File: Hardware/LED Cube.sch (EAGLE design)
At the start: 140 parts, among them IC1 MEGA32-P, IC10 FT232RL, IC11 FM24V10, IC12 MSGEQ7, IC13 MEGA8-P, IC2 74HC573N, IC3 74HC573N, IC4 74HC573N, IC5 74HC573N, IC6 74HC573N, IC7 74HC573N, IC8 74HC573N, IC9 74HC573N, Q2 BUZ382, Q3 BUZ382, Q4 BUZ382, Q5 BUZ382, Q6 BUZ382, Q7 BUZ382, Q8 BUZ382, Q9 BUZ382

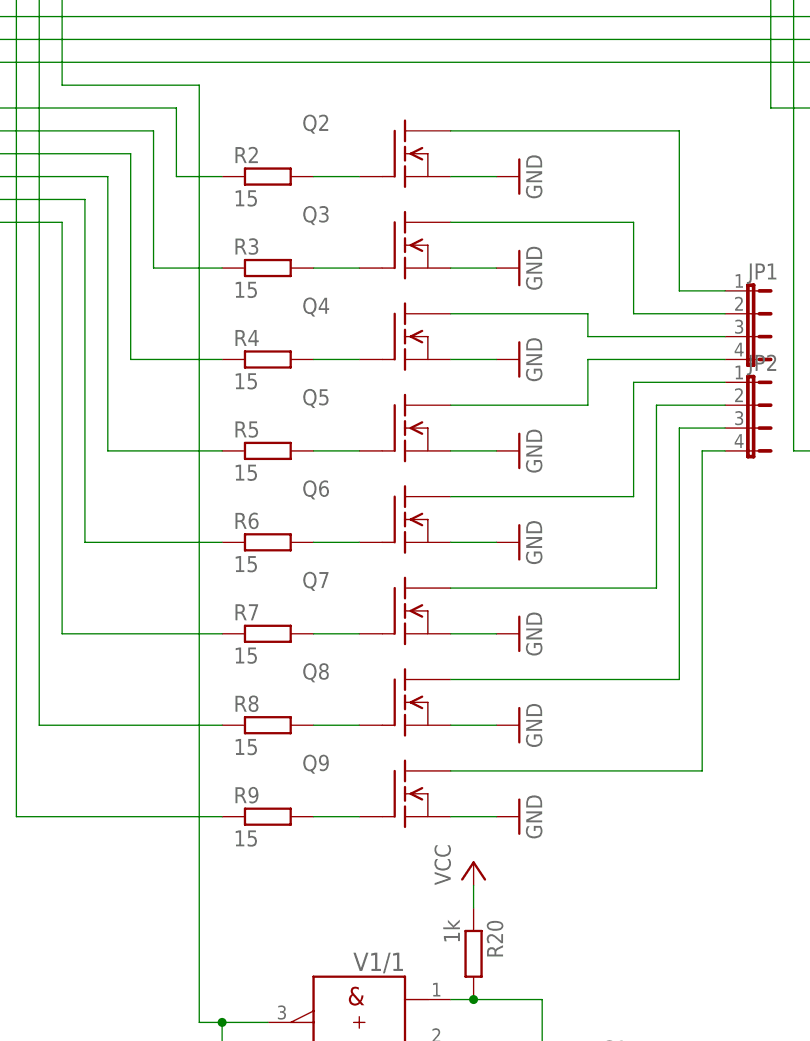
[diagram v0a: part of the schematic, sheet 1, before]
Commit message: Fixed MOSFET Problems
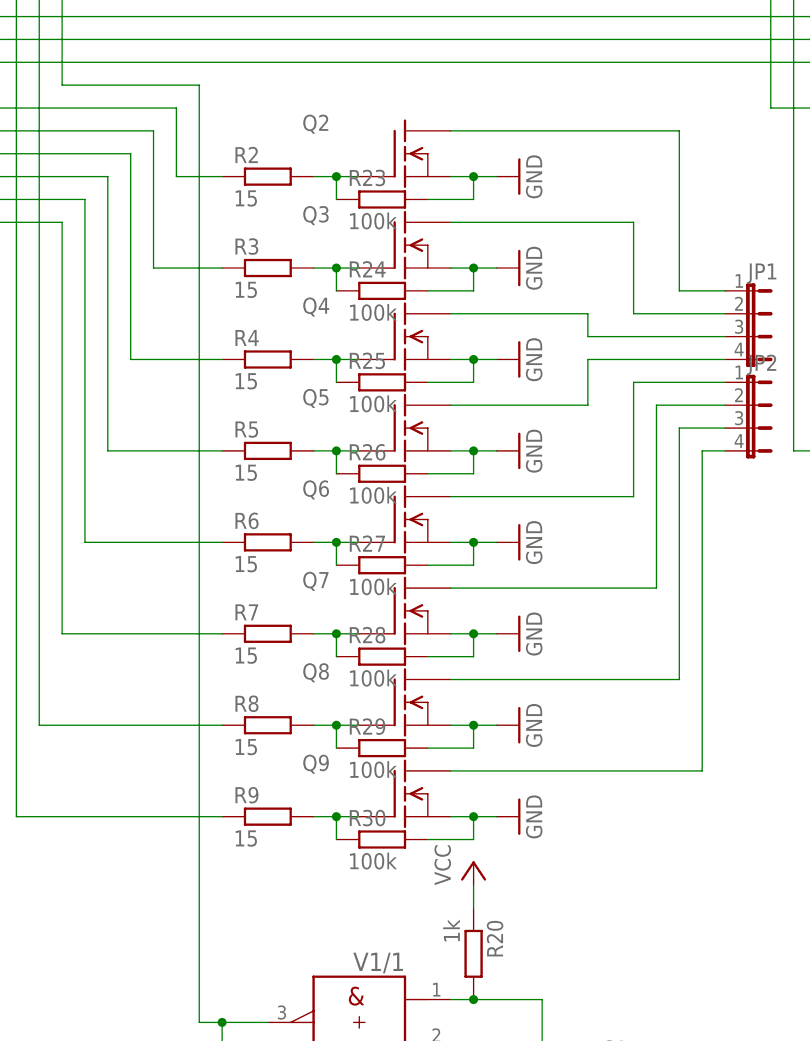
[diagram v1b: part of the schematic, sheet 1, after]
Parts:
- added R23, R24, R25, R26, R27, R28, R29, R30: 100k, resistor:R-EU_0204/7
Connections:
- net GND: now also R23.2, R24.2, R25.2, R26.2, R27.2, R28.2, R29.2, R30.2
- net N$22: now also R23.1
- net N$31: now also R24.1
- net N$32: now also R25.1
- net N$33: now also R26.1
- net N$34: now also R27.1
- net N$35: now also R28.1
- net N$36: now also R29.1
- net N$37: now also R30.1

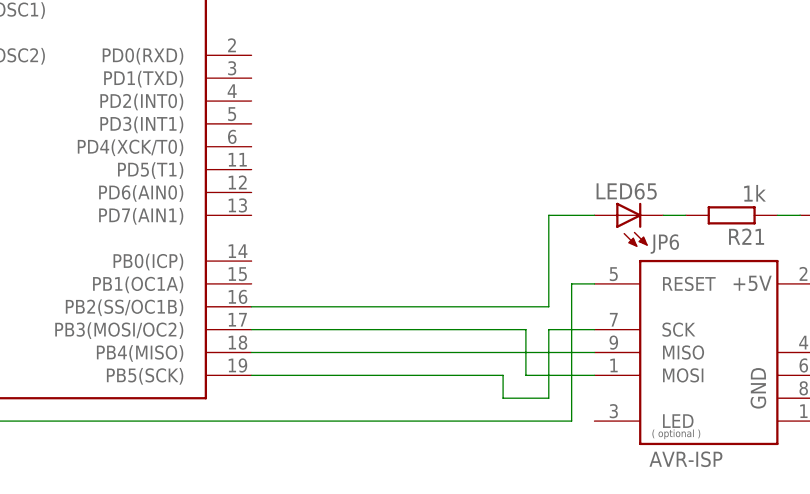
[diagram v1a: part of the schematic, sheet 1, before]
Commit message: Audio detection working
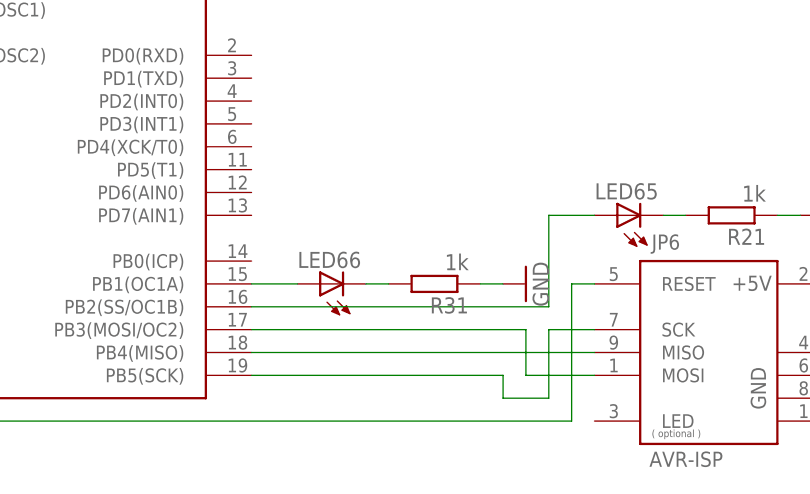
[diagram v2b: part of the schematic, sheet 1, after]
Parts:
- added LED66: (no value), led:LED5MM
- added R31: 1k, resistor:R-EU_0204/7
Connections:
- new net N$82: IC13.PB1(OC1A), LED66.A
- new net N$83: LED66.C, R31.2
- net GND: now also R31.1
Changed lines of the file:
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@@
 <setting verticaltext="up"/>
 </settings>
-<grid distance="0.1" unitdist="inch" unit="inch" style="lines" multiple="1" display="no" altdistance="0.05" altunitdist="inch" altunit="inch"/>
+<grid distance="0.1" unitdist="inch" unit="inch" style="lines" multiple="1" display="no" altdistance="0.01" altunitdist="inch" altunit="inch"/>
 <layers>
 <layer number="1" name="Top" color="4" fill="1" visible="no" active="no"/>
@@
 <part name="R29" library="resistor" deviceset="R-EU_" device="0204/7" value="100k"/>
 <part name="R30" library="resistor" deviceset="R-EU_" device="0204/7" value="100k"/>
+<part name="LED66" library="led" deviceset="LED" device="5MM"/>
+<part name="R31" library="resistor" deviceset="R-EU_" device="0204/7" value="1k"/>
+<part name="GND38" library="supply1" deviceset="GND" device=""/>
 </parts>
 <sheets>
@@
 <instance part="R29" gate="G$1" x="88.9" y="-43.18"/>
 <instance part="R30" gate="G$1" x="88.9" y="-53.34"/>
+<instance part="LED66" gate="G$1" x="-17.78" y="-124.46" rot="R90"/>
+<instance part="R31" gate="G$1" x="-5.08" y="-124.46" rot="R180"/>
+<instance part="GND38" gate="1" x="5.08" y="-124.46" rot="R90"/>
 </instances>
 <busses>
@@
 <pinref part="GND37" gate="1" pin="GND"/>
 <pinref part="R22" gate="G$1" pin="A"/>
+</segment>
+<segment>
+<pinref part="R31" gate="G$1" pin="1"/>
+<pinref part="GND38" gate="1" pin="GND"/>
+<wire x1="0" y1="-124.46" x2="2.54" y2="-124.46" width="0.1524" layer="91"/>
 </segment>
 </net>
@@
 </segment>
 </net>
+<net name="N$82" class="0">
+<segment>
+<pinref part="IC13" gate="G$1" pin="PB1(OC1A)"/>
+<pinref part="LED66" gate="G$1" pin="A"/>
+<wire x1="-25.4" y1="-124.46" x2="-20.32" y2="-124.46" width="0.1524" layer="91"/>
+</segment>
+</net>
+<net name="N$83" class="0">
+<segment>
+<pinref part="LED66" gate="G$1" pin="C"/>
+<pinref part="R31" gate="G$1" pin="2"/>
+<wire x1="-12.7" y1="-124.46" x2="-10.16" y2="-124.46" width="0.1524" layer="91"/>
+</segment>
+</net>

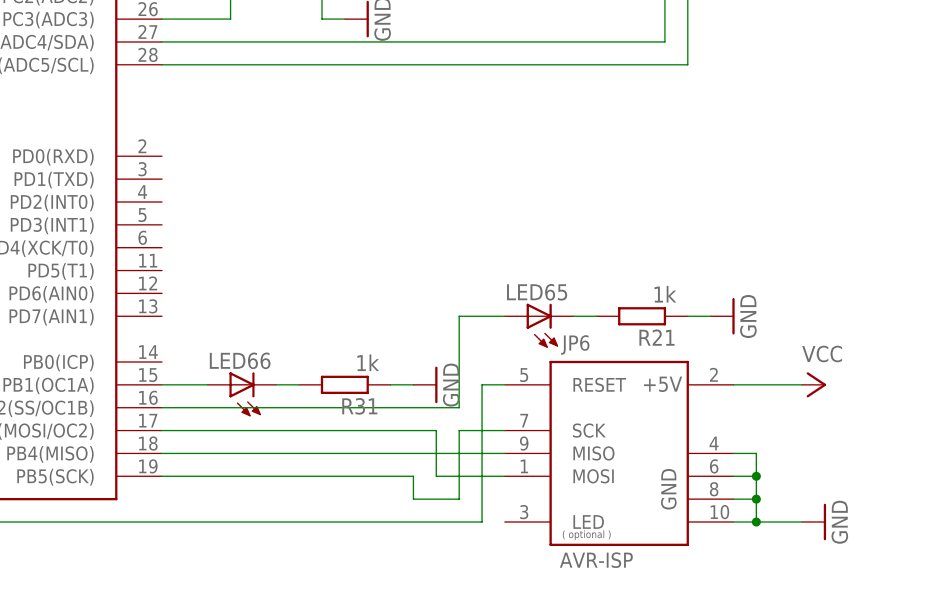
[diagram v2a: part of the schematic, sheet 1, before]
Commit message: Added LEDs to Audio Device
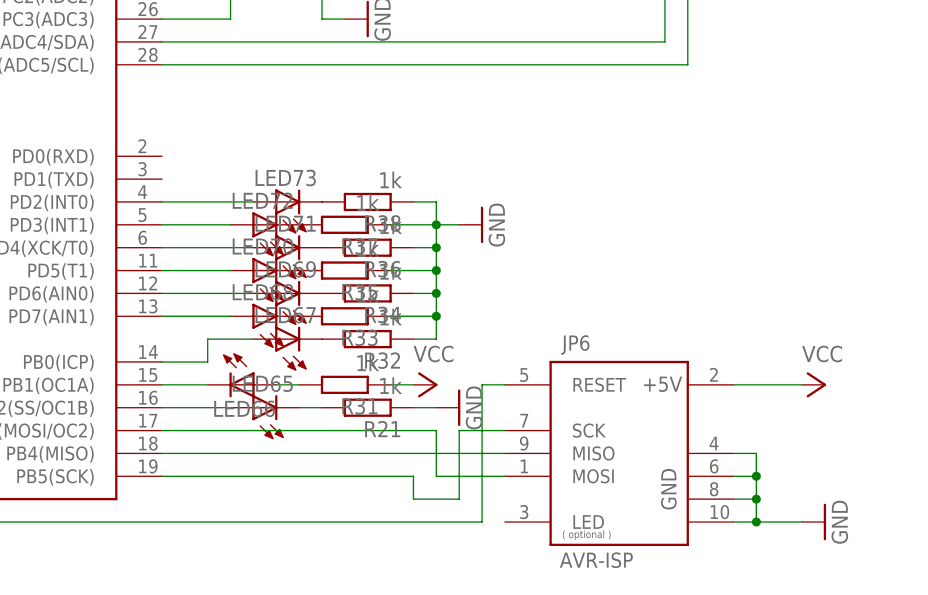
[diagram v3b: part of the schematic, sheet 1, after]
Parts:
- added LED67, LED68, LED69, LED70, LED71, LED72, LED73: (no value), led:LED5MM
- added R32, R33, R34, R35, R36, R37, R38: 1k, resistor:R-EU_0204/7
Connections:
- new net N$84: LED67.C, R32.2
- new net N$85: LED68.C, R33.2
- new net N$86: LED69.C, R34.2
- new net N$87: LED70.C, R35.2
- new net N$88: LED71.C, R36.2
- new net N$89: LED72.C, R37.2
- new net N$90: LED73.C, R38.2
- new net N$91: IC13.PB0(ICP), LED67.A
- new net N$92: IC13.PD7(AIN1), LED68.A
- new net N$93: IC13.PD6(AIN0), LED69.A
- new net N$94: IC13.PD5(T1), LED70.A
- new net N$95: IC13.PD4(XCK/T0), LED71.A
- new net N$96: IC13.PD3(INT1), LED72.A
- new net N$97: IC13.PD2(INT0), LED73.A
- net GND: now also R32.1, R33.1, R34.1, R35.1, R36.1, R37.1, R38.1; no longer R31.1
- net N$82: now also R31.2; no longer IC13.PB1(OC1A)
- net N$83: now also IC13.PB1(OC1A); no longer R31.2
- net VCC: now also R31.1
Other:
- moved on the sheet: LED65, LED66, R21

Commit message: Schematic ready for layout creation
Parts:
- removed CON1: (no value), con-harting:CON64
- removed IC13: MEGA8-P, 0-avr-6:MEGA8-P
- removed JP4, JP5: (no value), jumper:JP4E
- removed LED10, LED11, LED12, LED13, LED14, LED15, LED16, LED17, LED18, LED19, LED2, LED20, LED21, LED22, LED23, LED24, LED25, LED26, LED27, LED28, LED29, LED3, LED30, LED31, LED32, LED33, LED34, LED35, LED36, LED37, LED38, LED39, LED4, LED40, LED41, LED42, LED43, LED44, LED45, LED46, LED47, LED48, LED49, LED5, LED50, LED51, LED52, LED53, LED54, LED55, LED56, LED57, LED58, LED59, LED6, LED60, LED61, LED62, LED63, LED64, LED7, LED8, LED9: (no value), led:LED3MM
- removed LED66: (no value), led:LED5MM
- removed X1: (no value), con-berg:PN61729
- added IC14: MEGA32-A, atmel:MEGA32-A
- added R100, R101, R102, R39, R40, R41, R42, R43, R44, R45, R46, R47, R48, R49, R50, R51, R52, R53, R54, R55, R56, R57, R58, R59, R60, R61, R62, R63, R64, R65, R66, R67, R68, R69, R70, R71, R72, R73, R74, R75, R76, R77, R78, R79, R80, R81, R82, R83, R84, R85, R86, R87, R88, R89, R90, R91, R92, R93, R94, R95, R96, R97, R98, R99: 1k, resistor:R-EU_R0603
- added SV1: (no value), con-ml:ML64
- added U$10, U$11, U$12, U$13, U$14, U$15, U$16, U$17, U$18, U$19, U$20, U$21, U$22, U$23, U$24, U$25, U$26, U$27, U$28, U$29, U$3, U$30, U$31, U$32, U$33, U$34, U$35, U$36, U$37, U$38, U$39, U$4, U$40, U$41, U$42, U$43, U$44, U$45, U$46, U$47, U$48, U$49, U$5, U$50, U$51, U$52, U$53, U$54, U$55, U$56, U$57, U$58, U$59, U$6, U$60, U$61, U$62, U$63, U$64, U$65, U$7, U$8, U$9: PNP, 0-xythobuz:PNP
- added X2: USB-B-MINI-SMD, 1_USER:USB-B-MINI-SMD
- C1, C2, C3, C4, C5: device resistor:C-EU050-030X075 -> resistor:C-EUC0603
- C10, C11, C12, C13, C14, C15, C16, C17, C18, C6, C7, C8, C9: device resistor:C-EU050-025X075 -> resistor:C-EUC0603
- IC1: value MEGA32-P -> MEGA8-AI; device 0-avr-6:MEGA32-P -> atmel:MEGA8-AI
- IC2, IC3, IC4, IC5, IC6, IC7, IC8, IC9: value 74HC573N -> 74HC573D; device 74xx-eu:74HC573N -> 74xx-eu:74HC573D
- LED1: device led:LED3MM -> led:LEDCHIPLED_0603
- LED65, LED67, LED68, LED69, LED70, LED71, LED72, LED73: device led:LED5MM -> led:LEDCHIPLED_0603
- R1, R10, R11, R12, R13, R14, R15, R16, R17, R18, R19, R2, R20, R23, R24, R25, R26, R27, R28, R29, R3, R30, R4, R5, R6, R7, R8, R9: device resistor:R-EU_0204/7 -> resistor:R-EU_R0603
- U$2: value KLINKENBUCHSE -> PNP; device 0-xythobuz:KLINKENBUCHSE -> 0-xythobuz:PNP
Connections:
- removed net LEDA1: CON1.1, LED15.A
- removed net LEDA2: CON1.2, LED14.A
- removed net LEDA3: CON1.3, LED13.A
- removed net LEDA4: CON1.4, LED12.A
- removed net LEDA5: CON1.5, LED11.A
- removed net LEDA6: CON1.6, LED10.A
- removed net LEDA7: CON1.7, LED9.A
- removed net LEDA8: CON1.8, LED8.A
- new net N$100: SV1.5, U$4.C
- new net N$101: R44.2, U$7.B
- new net N$102: SV1.6, U$7.C
- new net N$103: R42.2, U$5.B
- new net N$104: SV1.8, U$9.C
- new net N$105: SV1.16, U$17.C
- new net N$106: R63.2, U$26.B
- new net N$107: R64.2, U$27.B
- new net N$108: R65.2, U$28.B
- new net N$109: SV1.12, U$11.C
- new net N$110: SV1.10, U$13.C
- new net N$111: SV1.9, U$10.C
- new net N$112: R54.2, U$17.B
- new net N$113: R63.1
- new net N$114: R64.1
- new net N$115: R66.2, U$29.B
- new net N$116: R66.1
- new net N$117: R67.2, U$30.B
- new net N$118: R67.1
- new net N$119: R65.1
- new net N$120: R68.2, U$31.B
- new net N$121: R71.2, U$34.B
- new net N$122: R72.2, U$35.B
- new net N$123: R73.2, U$36.B
- new net N$124: R71.1
- new net N$125: R72.1
- new net N$126: R74.2, U$37.B
- new net N$127: R74.1
- new net N$128: R75.2, U$38.B
- new net N$130: SV1.63, U$64.C
- new net N$131: SV1.61, U$60.C
- new net N$134: SV1.62, U$63.C
- new net N$136: SV1.58, U$61.C
- new net N$137: R95.2, U$58.B
- new net N$138: SV1.55, U$56.C
- new net N$139: R96.2, U$59.B
- new net N$140: R97.2, U$60.B
- new net N$141: R95.1
- new net N$142: SV1.54, U$55.C
- new net N$143: R96.1
- new net N$144: SV1.50, U$53.C
- new net N$145: R87.2, U$50.B
- new net N$146: R88.2, U$51.B
- new net N$147: R89.2, U$52.B
- new net N$148: R87.1
- new net N$149: R88.1
- new net N$150: R90.2, U$53.B
- new net N$151: R90.1
- new net N$152: R91.2, U$54.B
- new net N$153: R79.2, U$42.B
- new net N$154: R80.2, U$43.B
- new net N$155: R81.2, U$44.B
- new net N$156: R79.1
- new net N$157: R80.1
- new net N$158: R82.2, U$45.B
- new net N$159: R82.1
- new net N$160: R83.2, U$46.B
- new net N$161: R40.2, U$3.B
- new net N$162: R39.2, U$2.B
- new net N$163: IC7A.5Q, R41.1
- new net N$164: SV1.1, U$2.C
- new net N$165: R41.2, U$4.B
- new net N$166: SV1.7, U$8.C
- new net N$167: IC7A.1Q, R39.1
- new net N$168: IC7A.4Q, R40.1
- new net N$169: R47.2, U$10.B
- new net N$170: IC7A.6Q, R44.1
- new net N$171: R45.2, U$8.B
- new net N$172: IC7A.2Q, R42.1
- new net N$173: R43.2, U$6.B
- new net N$174: R48.2, U$11.B
- new net N$175: IC7A.3Q, R43.1
- new net N$176: IC7A.7Q, R45.1
- new net N$177: R46.2, U$9.B
- new net N$178: R49.2, U$12.B
- new net N$179: IC7A.8Q, R46.1
- new net N$180: R47.1
- new net N$181: R48.1
- new net N$182: R68.1
- new net N$183: SV1.13, U$12.C
- new net N$184: R50.2, U$13.B
- new net N$185: R50.1
- new net N$186: R51.2, U$14.B
- new net N$187: R51.1
- new net N$188: SV1.11, U$14.C
- new net N$189: R49.1
- new net N$190: R69.2, U$32.B
- new net N$191: R69.1
- new net N$192: R52.2, U$15.B
- new net N$193: R52.1
- new net N$194: SV1.14, U$15.C
- new net N$195: R53.2, U$16.B
- new net N$196: R53.1
- new net N$197: SV1.15, U$16.C
- new net N$198: R70.1
- new net N$199: SV1.32, U$33.C
- new net N$200: R54.1
- new net N$201: R55.2, U$18.B
- new net N$202: R56.2, U$19.B
- new net N$203: R57.2, U$20.B
- new net N$204: R55.1
- new net N$205: R56.1
- new net N$206: R58.2, U$21.B
- new net N$207: R58.1
- new net N$208: R59.2, U$22.B
- new net N$209: R59.1
- new net N$210: R57.1
- new net N$211: R60.2, U$23.B
- new net N$212: R60.1
- new net N$213: R61.2, U$24.B
- new net N$214: R61.1
- new net N$215: R62.1
- new net N$216: SV1.24, U$25.C
- new net N$217: SV1.23, U$24.C
- new net N$218: SV1.22, U$23.C
- new net N$219: SV1.21, U$20.C
- new net N$220: SV1.20, U$19.C
- new net N$221: SV1.18, U$21.C
- new net N$222: SV1.17, U$18.C
- new net N$223: R62.2, U$25.B
- new net N$224: SV1.19, U$22.C
- new net N$225: SV1.31, U$32.C
- new net N$226: SV1.30, U$31.C
- new net N$227: SV1.29, U$28.C
- new net N$228: SV1.28, U$27.C
- new net N$229: SV1.26, U$29.C
- new net N$230: SV1.25, U$26.C
- new net N$231: R70.2, U$33.B
- new net N$232: SV1.27, U$30.C
- new net N$233: R75.1
- new net N$234: R73.1
- new net N$235: R76.2, U$39.B
- new net N$236: R76.1
- new net N$237: R77.2, U$40.B
- new net N$238: R77.1
- new net N$239: R78.1
- new net N$240: SV1.40, U$41.C
- new net N$241: SV1.39, U$40.C
- new net N$242: SV1.38, U$39.C
- new net N$243: SV1.37, U$36.C
- new net N$244: SV1.36, U$35.C
- new net N$245: SV1.34, U$37.C
- new net N$246: SV1.33, U$34.C
- new net N$247: R78.2, U$41.B
- new net N$248: SV1.35, U$38.C
- new net N$249: R83.1
- new net N$250: R81.1
- new net N$251: R84.2, U$47.B
- new net N$252: R84.1
- new net N$253: R85.2, U$48.B
- new net N$254: R85.1
- new net N$255: R86.1
- new net N$256: SV1.48, U$49.C
- new net N$257: SV1.47, U$48.C
- new net N$258: SV1.46, U$47.C
- new net N$259: SV1.45, U$44.C
- new net N$260: SV1.44, U$43.C
- new net N$261: SV1.42, U$45.C
- new net N$262: SV1.41, U$42.C
- new net N$263: R86.2, U$49.B
- new net N$264: SV1.43, U$46.C
- new net N$265: R91.1
- new net N$266: R89.1
- new net N$267: R92.2, U$55.B
- new net N$268: R92.1
- new net N$269: R93.2, U$56.B
- new net N$270: R93.1
- new net N$271: R94.1
- new net N$272: SV1.56, U$57.C
- new net N$273: R98.2, U$61.B
- new net N$274: R98.1
- new net N$275: SV1.53, U$52.C
- new net N$276: SV1.52, U$51.C
- new net N$277: R99.2, U$62.B
- new net N$278: SV1.49, U$50.C
- new net N$279: R94.2, U$57.B
- new net N$280: SV1.51, U$54.C
- new net N$281: R99.1
- new net N$282: R97.1
- new net N$283: R100.2, U$63.B
- new net N$284: R100.1
- new net N$285: R101.2, U$64.B
- new net N$286: R101.1
- new net N$287: R102.1
- new net N$288: SV1.64, U$65.C
- new net N$292: SV1.60, U$59.C
- new net N$294: SV1.57, U$58.C
- new net N$295: R102.2, U$65.B
- new net N$296: SV1.59, U$62.C
- new net N$98: SV1.2, U$5.C
- new net N$99: SV1.3, U$6.C
- net GND: now also IC1.GND@1, IC1.GND@2, IC14.GND, IC14.GND1, IC14.GND2, IC14.GND@1, R31.1, X2-CON.5; no longer IC1.AGND, IC13.AGND, IC13.GND@1, U$2.GND, X1.4
- net N$1: now also SV1.4, U$3.C; no longer JP4.4, LED1.C, LED10.C, LED11.C, LED12.C, LED13.C, LED14.C, LED15.C, LED16.C, LED17.C, LED18.C, LED19.C, LED2.C, LED20.C, LED21.C, LED22.C, LED23.C, LED24.C, LED25.C, LED26.C, LED27.C, LED28.C, LED29.C, LED3.C, LED30.C, LED31.C, LED32.C, LED33.C, LED34.C, LED35.C, LED36.C, LED37.C, LED38.C, LED39.C, LED4.C, LED40.C, LED41.C, LED42.C, LED43.C, LED44.C, LED45.C, LED46.C, LED47.C, LED48.C, LED49.C, LED5.C, LED50.C, LED51.C, LED52.C, LED53.C, LED54.C, LED55.C, LED56.C, LED57.C, LED58.C, LED59.C, LED6.C, LED60.C, LED61.C, LED62.C, LED63.C, LED64.C, LED7.C, LED8.C, LED9.C
- net N$10: now also IC14.(ADC4)PA4; no longer IC1.(ADC4)PA4
- net N$11: now also IC14.(ADC5)PA5; no longer IC1.(ADC5)PA5
- net N$12: now also IC14.(ADC6)PA6; no longer IC1.(ADC6)PA6
- net N$13: now also IC14.(ADC7)PA7; no longer IC1.(ADC7)PA7
- net N$14: now also IC14.(T1)PB1; no longer IC1.(T1)PB1
- net N$15: now also IC14.(AIN0/INT2)PB2; no longer IC1.(AIN0/INT2)PB2
- net N$16: now also IC14.(TCK)PC2; no longer IC1.(TCK)PC2
- net N$17: now also IC14.(TMS)PC3; no longer IC1.(TMS)PC3
- net N$18: now also IC14.(TDO)PC4; no longer IC1.(TDO)PC4
- net N$19: now also IC14.(TDI)PC5; no longer IC1.(TDI)PC5
- net N$2: now also IC14.RESET; no longer IC1.RESET
- net N$20: now also IC14.(TOSC1)PC6; no longer IC1.(TOSC1)PC6
- net N$21: now also IC14.(TOSC2)PC7; no longer IC1.(TOSC2)PC7
- net N$23: now also IC14.(OC2)PD7; no longer IC1.(OC2)PD7
- net N$24: now also IC14.(ICP)PD6; no longer IC1.(ICP)PD6
- net N$25: now also IC14.(OC1A)PD5; no longer IC1.(OC1A)PD5
- net N$26: now also IC14.(OC1B)PD4; no longer IC1.(OC1B)PD4
- net N$27: now also IC14.(INT1)PD3; no longer IC1.(INT1)PD3
- net N$28: now also IC14.(INT0)PD2; no longer IC1.(INT0)PD2
- net N$29: now also IC14.(SS)PB4; no longer IC1.(SS)PB4
- net N$3: now also IC14.AREF; no longer IC1.AREF
- net N$30: now also IC14.(AIN1/OC0)PB3; no longer IC1.(AIN1/OC0)PB3
- net N$4: now also IC14.(ADC0)PA0; no longer IC1.(ADC0)PA0
- net N$46: now also X2-CON.1; no longer X1.1
- net N$47: now also IC14.(SCK)PB7; no longer IC1.(SCK)PB7
- net N$48: now also IC14.(MISO)PB6; no longer IC1.(MISO)PB6
- net N$49: now also IC14.(MOSI)PB5; no longer IC1.(MOSI)PB5
- net N$5: now also IC14.(ADC1)PA1; no longer IC1.(ADC1)PA1
- net N$50: now also IC14.(TXD)PD1; no longer IC1.(TXD)PD1
- net N$51: now also IC14.(RXD)PD0; no longer IC1.(RXD)PD0
- net N$53: now also IC1.PC4(ADC4/SDA), IC14.PC1(SDA); no longer IC1.(SDA)PC1, IC13.PC4(ADC4/SDA)
- net N$54: now also X2-CON.3; no longer X1.3
- net N$56: now also X2-CON.2; no longer X1.2
- net N$57: now also IC1.PC5(ADC5/SCL), IC14.PC0(SCL); no longer IC1.(SCL)PC0, IC13.PC5(ADC5/SCL)
- net N$6: now also IC14.(ADC2)PA2; no longer IC1.(ADC2)PA2
- net N$63: no longer U$2.R
- net N$64: no longer U$2.L
- net N$65: now also IC1.PC0(ADC0); no longer IC13.PC0(ADC0)
- net N$66: now also IC1.PC6(/RESET); no longer IC13.PC6(/RESET)
- net N$67: now also IC1.PC2(ADC2); no longer IC13.PC2(ADC2)
- net N$68: now also IC1.PC3(ADC3); no longer IC13.PC3(ADC3)
- net N$69: now also IC14.(T0/XCK)PB0; no longer IC1.(T0/XCK)PB0
- net N$7: now also IC14.XTAL2; no longer IC1.XTAL2
- net N$70: now also IC1.PB7(XTAL2/TOSC2); no longer IC13.PB7(XTAL2/TOSC2)
- net N$71: now also IC1.PB6(XTAL1/TOSC1); no longer IC13.PB6(XTAL1/TOSC1)
- net N$75: now also IC1.PB2(SS/OC1B); no longer IC13.PB2(SS/OC1B)
- net N$77: now also IC1.PC1(ADC1); no longer IC13.PC1(ADC1)
- net N$78: now also IC1.AREF; no longer IC13.AREF
- net N$79: now also IC1.PB4(MISO); no longer IC13.PB4(MISO)
- net N$8: now also IC14.XTAL1; no longer IC1.XTAL1
- net N$80: now also IC1.PB3(MOSI/OC2); no longer IC13.PB3(MOSI/OC2)
- net N$81: now also IC1.PB5(SCK); no longer IC13.PB5(SCK)
- net N$82: now also LED1.C; no longer LED66.A
- net N$83: now also IC1.PB1(OC1A), LED1.A; no longer IC13.PB1(OC1A), LED66.C
- net N$9: now also IC14.(ADC3)PA3; no longer IC1.(ADC3)PA3
- net N$91: now also IC1.PB0(ICP); no longer IC13.PB0(ICP)
- net N$92: now also IC1.PD7(AIN1); no longer IC13.PD7(AIN1)
- net N$93: now also IC1.PD6(AIN0); no longer IC13.PD6(AIN0)
- net N$94: now also IC1.PD5(T1); no longer IC13.PD5(T1)
- net N$95: now also IC1.PD4(XCK/T0); no longer IC13.PD4(XCK/T0)
- net N$96: now also IC1.PD3(INT1); no longer IC13.PD3(INT1)
- net N$97: now also IC1.PD2(INT0); no longer IC13.PD2(INT0)
- net VCC: now also IC1.VCC@1, IC1.VCC@2, IC14.AVCC, IC14.VCC, IC14.VCC1, IC14.VCC2, U$10.E, U$11.E, U$12.E, U$13.E, U$14.E, U$15.E, U$16.E, U$17.E, U$18.E, U$19.E, U$2.E, U$20.E, U$21.E, U$22.E, U$23.E, U$24.E, U$25.E, U$26.E, U$27.E, U$28.E, U$29.E, U$3.E, U$30.E, U$31.E, U$32.E, U$33.E, U$34.E, U$35.E, U$36.E, U$37.E, U$38.E, U$39.E, U$4.E, U$40.E, U$41.E, U$42.E, U$43.E, U$44.E, U$45.E, U$46.E, U$47.E, U$48.E, U$49.E, U$5.E, U$50.E, U$51.E, U$52.E, U$53.E, U$54.E, U$55.E, U$56.E, U$57.E, U$58.E, U$59.E, U$6.E, U$60.E, U$61.E, U$62.E, U$63.E, U$64.E, U$65.E, U$7.E, U$8.E, U$9.E; no longer IC1.VCC, IC13.AVCC, IC13.VCC@1, R31.1
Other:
- note added: "1"
- note added: "2"
- note added: "3"
- note added: "4"
- note added: "5"
- note added: "6"
- note added: "7"
- note added: "8"
- note removed: "Eine Ebene des LED Würfels als Beispiel"
- note removed: "Und so weiter"

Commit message: Schematic fix
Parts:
- removed JP2: (no value), jumper:JP4E
- JP1: device jumper:JP4E -> 0-roboternetz-definitionen:PORT
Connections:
- removed net N$180 (its old number): R47.1
- removed net N$181 (its old number): R48.1
- removed net N$204 (its old number): R55.1
- removed net N$205 (its old number): R56.1
- removed net N$40: JP1.3, Q4.D
- removed net N$41: JP1.4, Q5.D
- new net N$133: IC2A.1Q, R47.1
- new net N$135: IC2A.4Q, R48.1
- new net N$167: IC3A.1Q, R55.1
- new net N$168: IC3A.4Q, R56.1
- new net N$278: JP1.P2, Q4.D
- new net N$289: JP1.P3, Q5.D
- net GND: now also JP1.GND
- net N$113: now also IC4A.1Q
- net N$114: now also IC4A.4Q
- net N$116: now also IC4A.2Q
- net N$118: now also IC4A.3Q
- net N$119: now also IC4A.5Q
- net N$124: now also IC5A.1Q
- net N$125: now also IC5A.4Q
- net N$127: now also IC5A.2Q
- net N$141: now also IC9A.1Q
- net N$143: now also IC9A.4Q
- net N$148: now also IC8A.4Q, R88.1; no longer R87.1
- net N$149: now also IC8A.1Q, R87.1; no longer R88.1
- net N$151: now also IC8A.2Q
- net N$156: now also IC6A.1Q
- net N$157: now also IC6A.4Q
- net N$159: now also IC6A.2Q
- net N$182: now also IC4A.6Q
- net N$185: now also IC2A.2Q
- net N$187: now also IC2A.3Q
- net N$189: now also IC2A.5Q
- net N$191: now also IC4A.7Q
- net N$193: now also IC2A.6Q
- net N$196: now also IC2A.7Q
- net N$198: now also IC4A.8Q
- net N$200: now also IC2A.8Q
- net N$207: now also IC3A.2Q
- net N$209: now also IC3A.3Q
- net N$210: now also IC3A.5Q
- net N$212: now also IC3A.6Q
- net N$214: now also IC3A.7Q
- net N$215: now also IC3A.8Q
- net N$233: now also IC5A.3Q
- net N$234: now also IC5A.5Q
- net N$236: now also IC5A.6Q
- net N$238: now also IC5A.7Q
- net N$239: now also IC5A.8Q
- net N$249: now also IC6A.3Q
- net N$250: now also IC6A.5Q
- net N$252: now also IC6A.6Q
- net N$254: now also IC6A.7Q
- net N$255: now also IC6A.8Q
- net N$265: now also IC8A.3Q
- net N$266: now also IC8A.5Q
- net N$268: now also IC8A.6Q
- net N$270: now also IC8A.7Q
- net N$271: now also IC8A.8Q
- net N$274: now also IC9A.2Q
- net N$281: now also IC9A.3Q
- net N$282: now also IC9A.5Q
- net N$284: now also IC9A.6Q
- net N$286: now also IC9A.7Q
- net N$287: now also IC9A.8Q
- net N$38: now also JP1.P0; no longer JP1.1
- net N$39: now also JP1.P1; no longer JP1.2
- net N$42: now also JP1.P4; no longer JP2.1
- net N$43: now also JP1.P5; no longer JP2.2
- net N$44: now also JP1.P6; no longer JP2.3
- net N$45: now also JP1.P7; no longer JP2.4
- net VCC: now also JP1.VCC

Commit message: Started layouting
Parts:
- removed LED67, LED68, LED69, LED70, LED71, LED72, LED73: (no value), led:LEDCHIPLED_0603
- removed Q2, Q3, Q4, Q5, Q6, Q7, Q8, Q9: BUZ382, transistor-fet:BUZ382
- removed R32, R33, R34, R35, R36, R37, R38: 1k, resistor:R-EU_0204/7
- added U$66, U$67, U$68, U$69, U$70, U$71, U$72, U$73: IRF530, 0-xythobuz:IRF530
- R21, R31: device resistor:R-EU_0204/7 -> resistor:R-EU_R0603
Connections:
- removed net N$84: LED67.C, R32.2
- removed net N$85: LED68.C, R33.2
- removed net N$86: LED69.C, R34.2
- removed net N$87: LED70.C, R35.2
- removed net N$88: LED71.C, R36.2
- removed net N$89: LED72.C, R37.2
- removed net N$90: LED73.C, R38.2
- removed net N$91: IC1.PB0(ICP), LED67.A
- removed net N$92: IC1.PD7(AIN1), LED68.A
- removed net N$93: IC1.PD6(AIN0), LED69.A
- removed net N$94: IC1.PD5(T1), LED70.A
- removed net N$95: IC1.PD4(XCK/T0), LED71.A
- removed net N$96: IC1.PD3(INT1), LED72.A
- removed net N$97: IC1.PD2(INT0), LED73.A
- net GND: now also U$66.S, U$67.S, U$68.S, U$69.S, U$70.S, U$71.S, U$72.S, U$73.S, V1/-UB.-UB; no longer Q2.S, Q3.S, Q4.S, Q5.S, Q6.S, Q7.S, Q8.S, Q9.S, R32.1, R33.1, R34.1, R35.1, R36.1, R37.1, R38.1
- net N$22: now also U$66.G; no longer Q2.G
- net N$278: now also U$68.D; no longer Q4.D
- net N$289: now also U$69.D; no longer Q5.D
- net N$31: now also U$67.G; no longer Q3.G
- net N$32: now also U$68.G; no longer Q4.G
- net N$33: now also U$69.G; no longer Q5.G
- net N$34: now also U$70.G; no longer Q6.G
- net N$35: now also U$71.G; no longer Q7.G
- net N$36: now also U$72.G; no longer Q8.G
- net N$37: now also U$73.G; no longer Q9.G
- net N$38: now also U$66.D; no longer Q2.D
- net N$39: now also U$67.D; no longer Q3.D
- net N$42: now also U$70.D; no longer Q6.D
- net N$43: now also U$71.D; no longer Q7.D
- net N$44: now also U$72.D; no longer Q8.D
- net N$45: now also U$73.D; no longer Q9.D
- net VCC: now also V1/+UB.+UB
